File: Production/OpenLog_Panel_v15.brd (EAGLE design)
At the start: 202.2 x 111 mm, 1503 parts, among them Q1 16MHZ, Q10 16MHZ, Q11 16MHZ, Q12 16MHZ, Q13 16MHZ, Q14 16MHZ, Q15 16MHZ, Q16 16MHZ, Q17 16MHZ, Q18 16MHZ, Q19 16MHZ, Q2 16MHZ, Q20 16MHZ, Q21 16MHZ, Q22 16MHZ, Q23 16MHZ, Q24 16MHZ, Q25 16MHZ, Q26 16MHZ, Q27 16MHZ, Q28 16MHZ, Q29 16MHZ, Q3 16MHZ, Q30 16MHZ, Q31 16MHZ, Q32 16MHZ, Q33 16MHZ, Q34 16MHZ, Q35 16MHZ, Q36 16MHZ, Q37 16MHZ, Q38 16MHZ, Q39 16MHZ, Q4 16MHZ, Q40 16MHZ, Q41 16MHZ, Q42 16MHZ, Q43 16MHZ, Q44 16MHZ, Q45 16MHZ, Q46 16MHZ, Q47 16MHZ, Q48 16MHZ, Q49 16MHZ, Q5 16MHZ, Q50 16MHZ, Q51 16MHZ, Q52 16MHZ, Q53 16MHZ, Q54 16MHZ, Q55 16MHZ, Q56 16MHZ, Q57 16MHZ, Q58 16MHZ, Q59 16MHZ, Q6 16MHZ, Q60 16MHZ, Q7 16MHZ, Q8 16MHZ, Q9 16MHZ, U1 ATMEGA328P_TQFP, U10 3.3V MIC5205, U100 3.3V MIC5205, U101 microSD Socket, U102 ATMEGA328P_TQFP, U103 3.3V MIC5205, U104 microSD Socket, U105 ATMEGA328P_TQFP, U106 3.3V MIC5205, U107 microSD Socket, U108 ATMEGA328P_TQFP, U109 3.3V MIC5205, U11 microSD Socket, U110 microSD Socket, U111 ATMEGA328P_TQFP, U112 3.3V MIC5205, U113 microSD Socket, U114 ATMEGA328P_TQFP, U115 3.3V MIC5205, U116 microSD Socket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

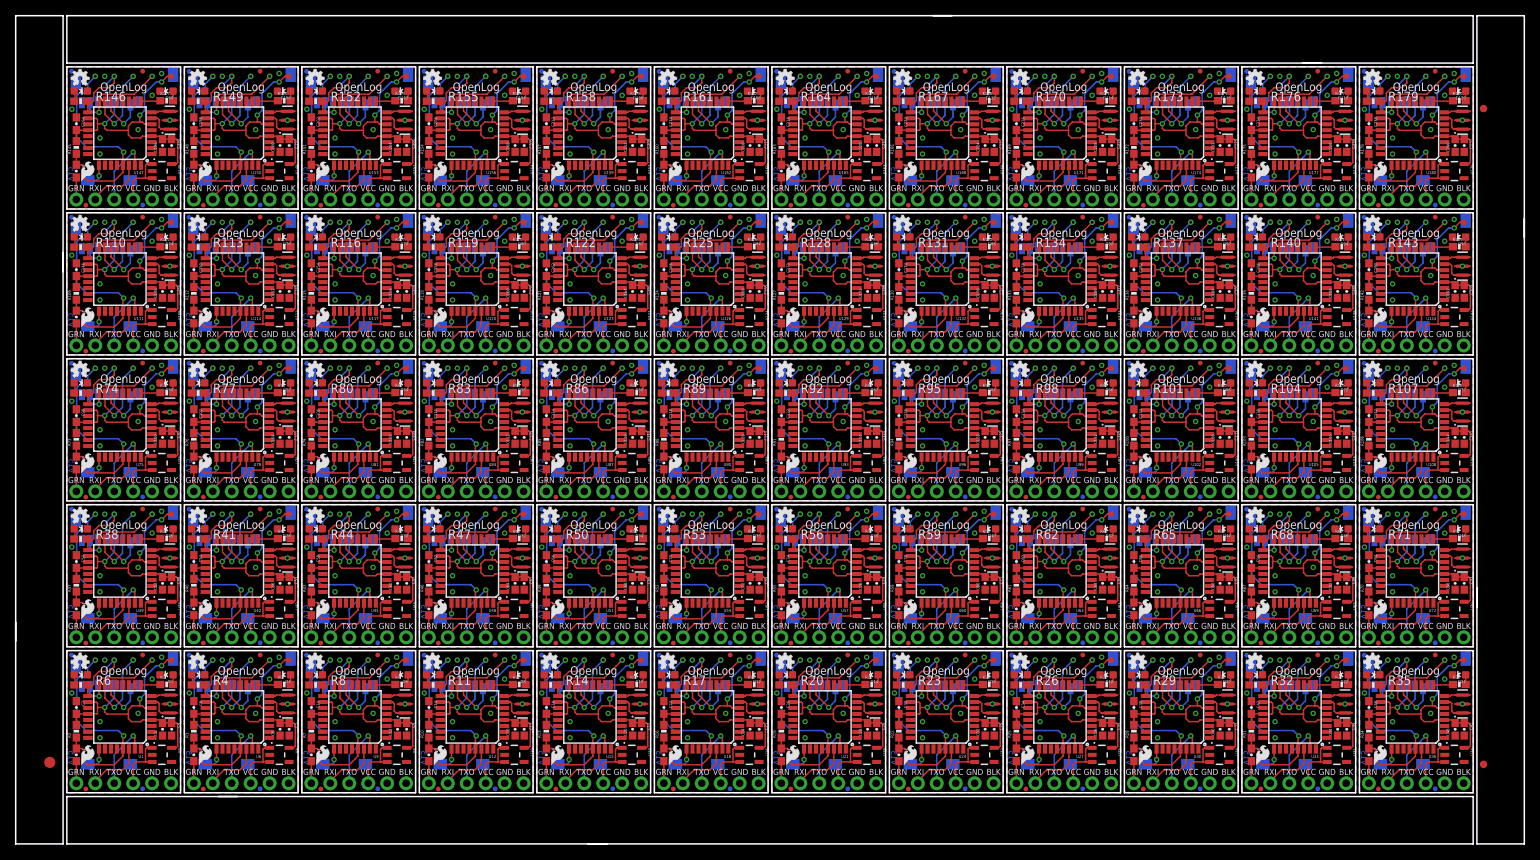
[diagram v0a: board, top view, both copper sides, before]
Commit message: added bottom side panel fiducials
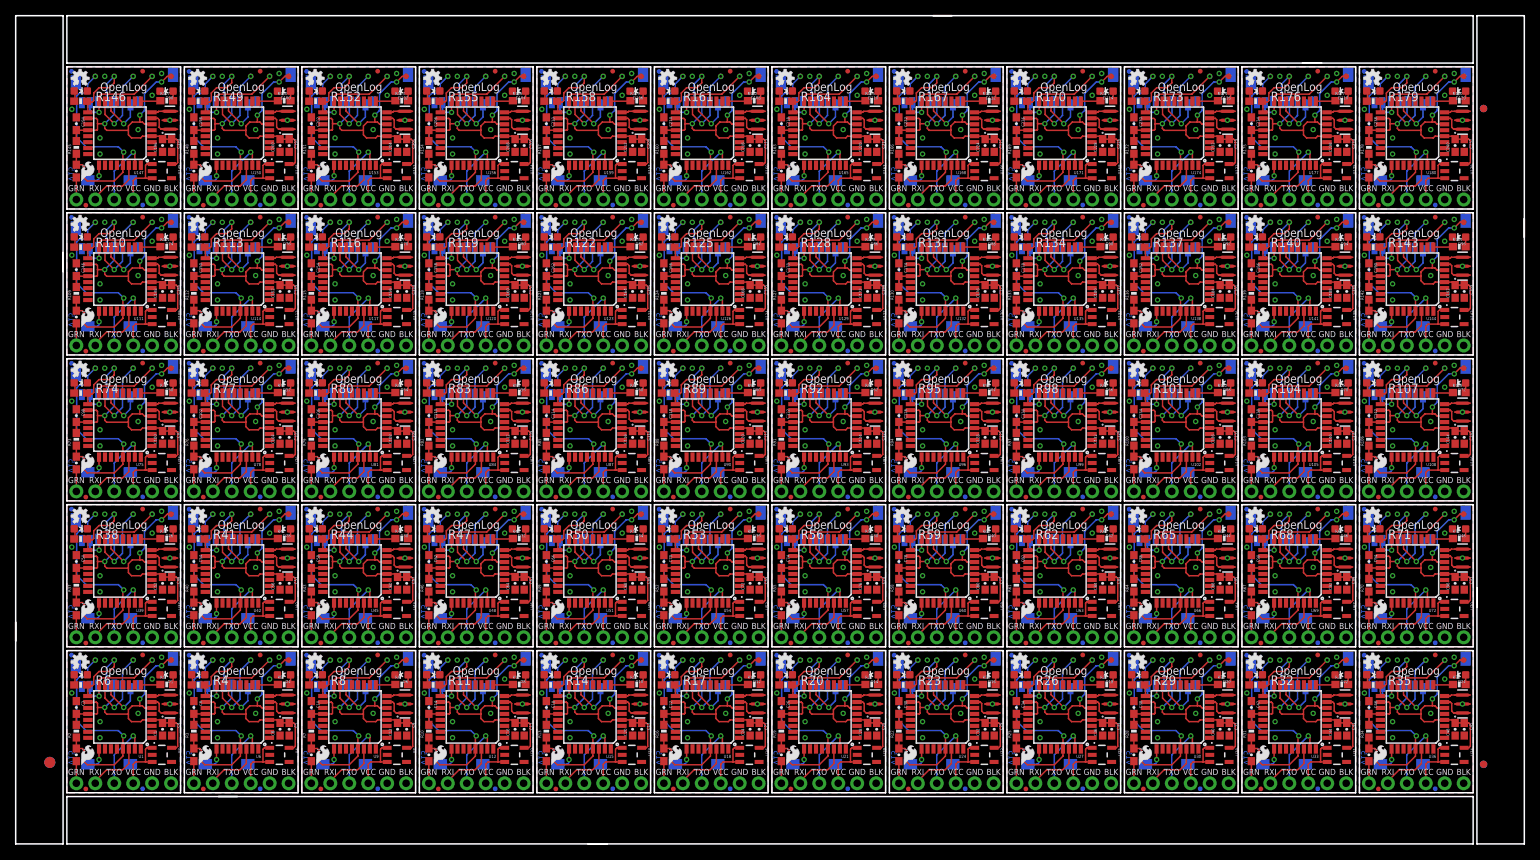
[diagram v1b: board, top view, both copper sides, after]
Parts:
- added E$2: (no value), SparkFun-Retired:FIDUCIAL-1.5X3
- added E$3, E$4: (no value), SparkFun-Aesthetics:FIDUCIAL-1X2
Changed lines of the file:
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@@
 <element name="E$8" library="SparkFun-Aesthetics" package="FIDUCIAL-1X2" value="" x="196.723" y="10.668"/>
 <element name="E$1" library="SparkFun-Retired" package="FIDUCIAL-1.5X3" value="" x="4.572" y="10.922"/>
+<element name="E$2" library="SparkFun-Retired" package="FIDUCIAL-1.5X3" value="" x="4.572" y="10.922" rot="MR0"/>
+<element name="E$3" library="SparkFun-Aesthetics" package="FIDUCIAL-1X2" value="" x="196.723" y="10.668" rot="MR0"/>
+<element name="E$4" library="SparkFun-Aesthetics" package="FIDUCIAL-1X2" value="" x="196.723" y="98.552" rot="MR180"/>
 </elements>
 <signals>
